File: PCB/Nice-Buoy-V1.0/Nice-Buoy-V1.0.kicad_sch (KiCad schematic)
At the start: 0 parts

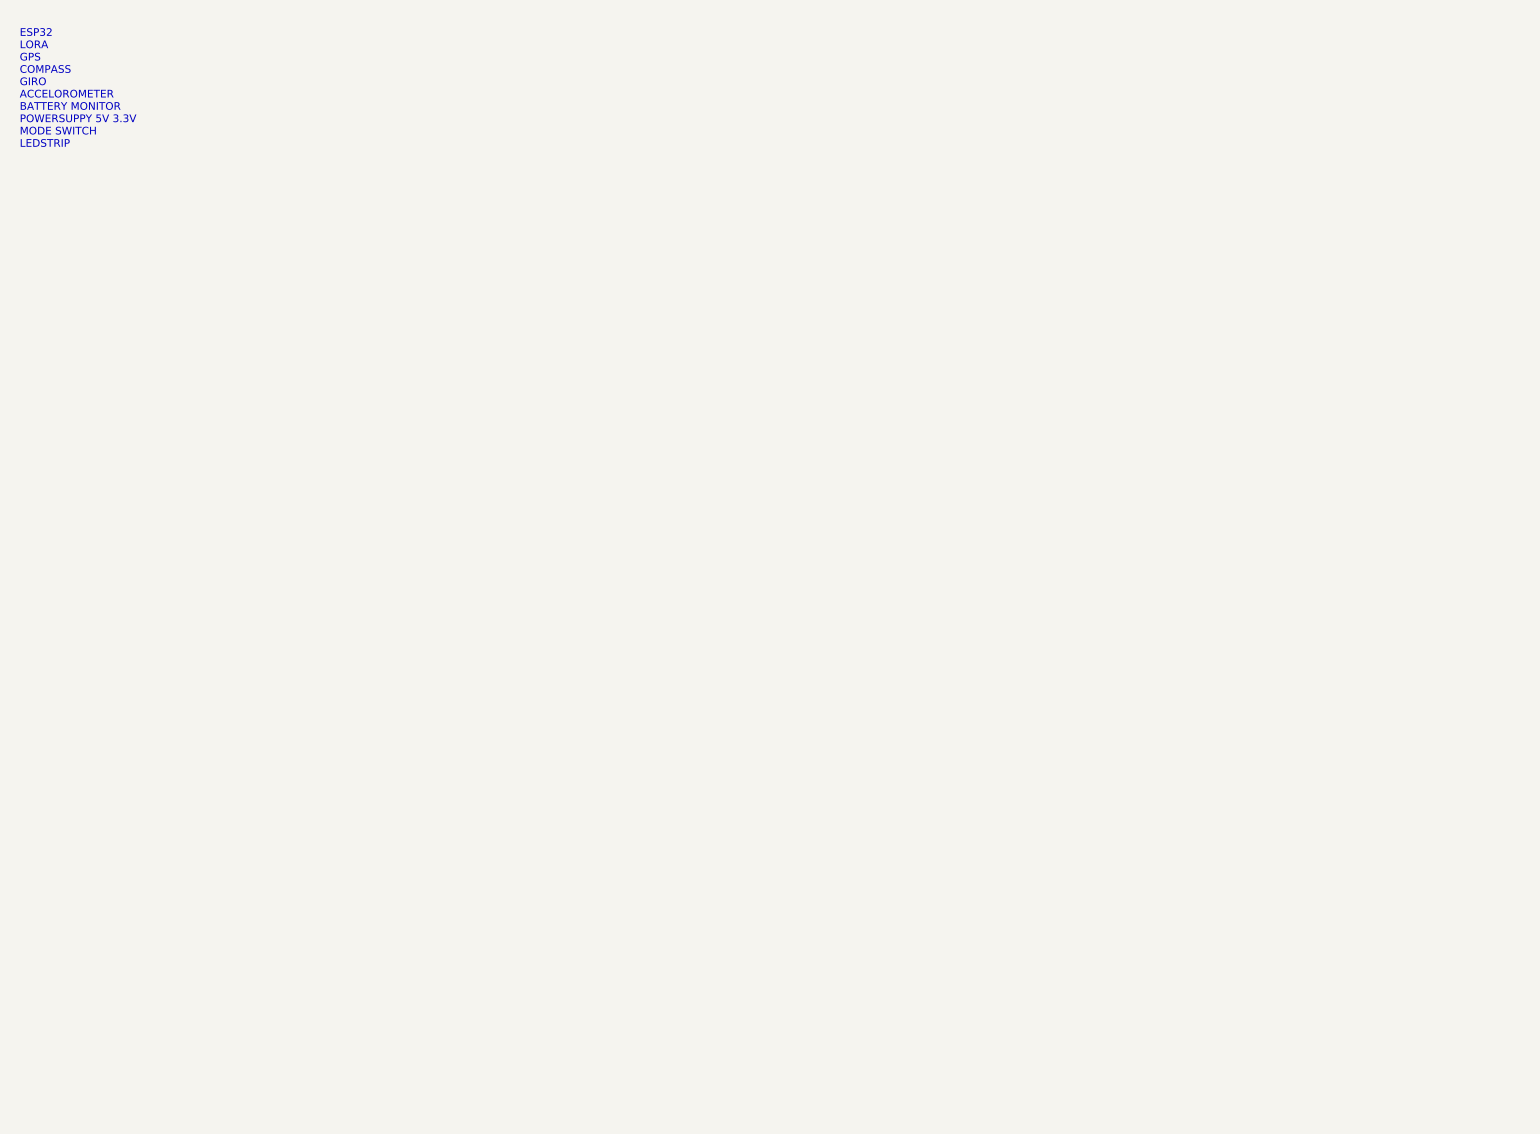
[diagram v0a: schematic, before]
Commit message: Compass BM150 is not okl. Next commit with LSM303
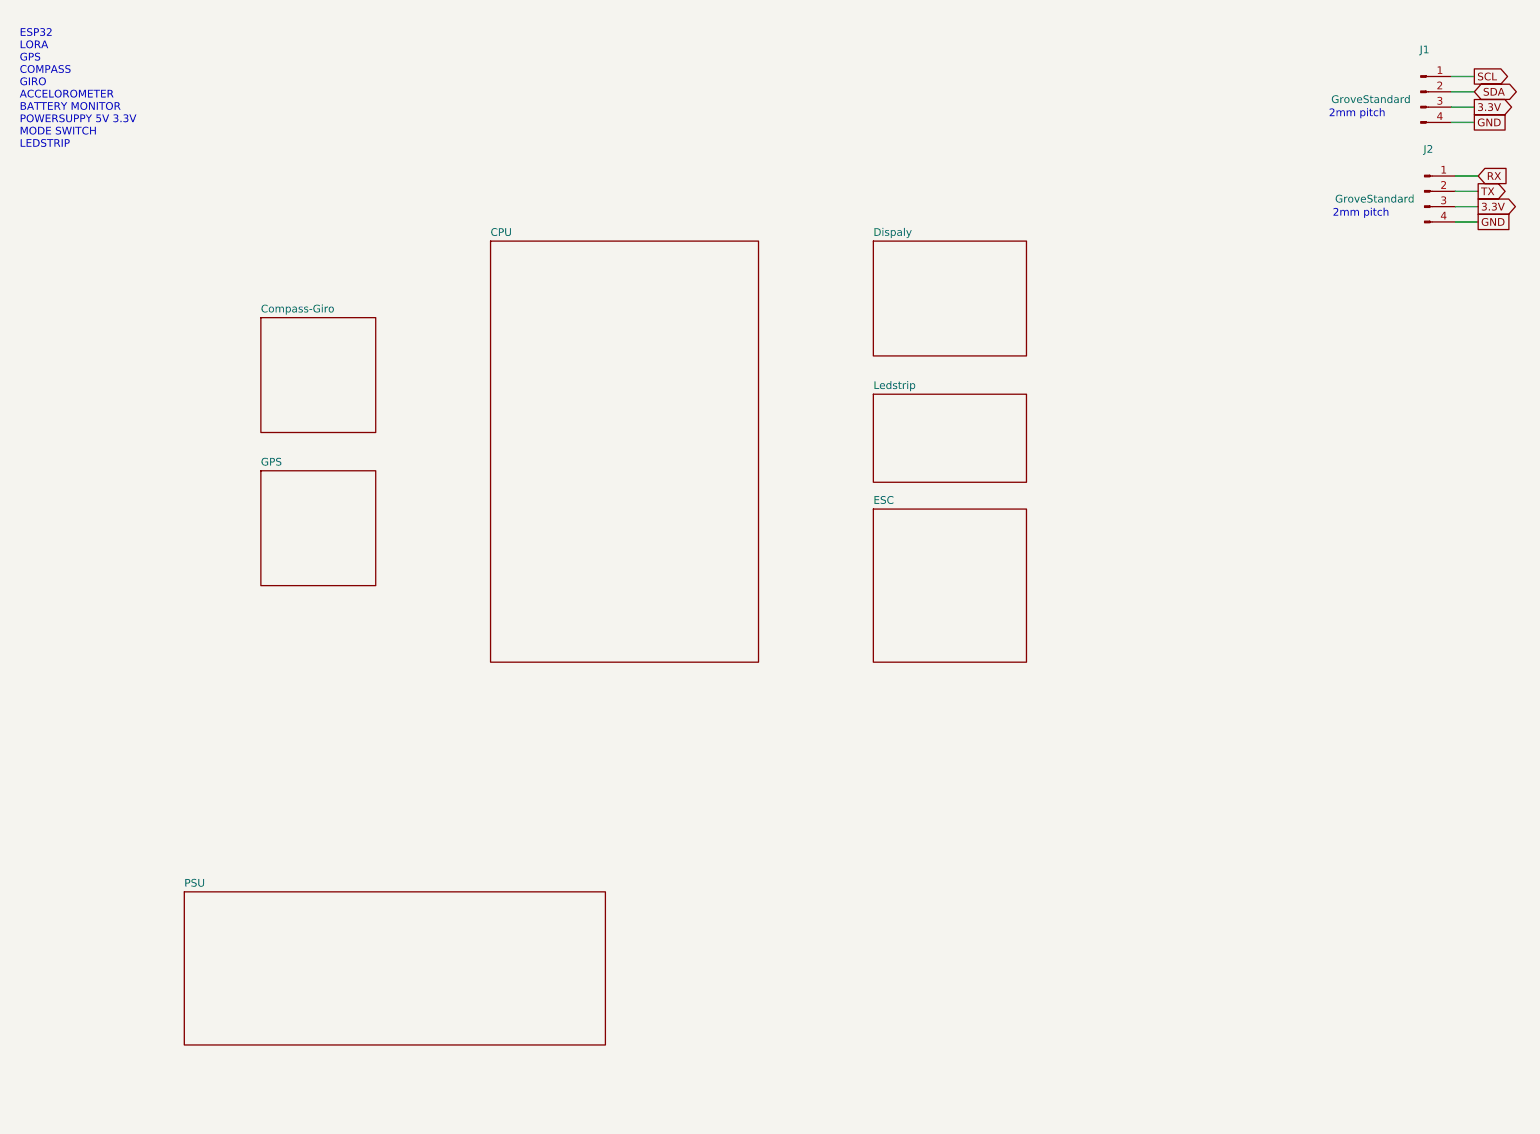
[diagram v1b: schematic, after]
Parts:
- added J1, J2: GroveStandard, symbol Connector:Conn_01x04_Pin
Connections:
- new net 3.3V: J1.3 (Pin_3), J2.3 (Pin_3)
- new net GND: J1.4 (Pin_4), J2.4 (Pin_4)
- new net RX: J2.1 (Pin_1)
- new net SCL: J1.1 (Pin_1)
- new net SDA: J1.2 (Pin_2)
- new net TX: J2.2 (Pin_2)
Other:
- added sheet CPU (CPU_sch.kicad_sch)
- added sheet Compass-Giro (Compass_sch.kicad_sch)
- added sheet Dispaly (Display_sch.kicad_sch)
- added sheet ESC (Esc_sch.kicad_sch)
- added sheet GPS (Gps_sch.kicad_sch)
- added sheet Ledstrip (Ledstrip_sch.kicad_sch)
- added sheet PSU (PSU_sch.kicad_sch)
- note added: "2mm pitch"
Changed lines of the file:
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@@
     (company "NicE Engineering")
+  )
+  (wire (pts (xy 255.27 40.005) (xy 259.08 40.005))
+    (stroke (width 0) (type default))
+  )
+  (wire (pts (xy 255.27 42.545) (xy 259.08 42.545))
+    (stroke (width 0) (type default))
+  )
+  (wire (pts (xy 254.635 26.035) (xy 258.445 26.035))
+    (stroke (width 0) (type default))
+  )
+  (wire (pts (xy 255.27 45.085) (xy 259.08 45.085))
+    (stroke (width 0) (type default))
+  )
+  (wire (pts (xy 254.635 28.575) (xy 258.445 28.575))
+    (stroke (width 0) (type default))
+  )
+  (wire (pts (xy 255.27 47.625) (xy 259.08 47.625))
+    (stroke (width 0) (type default))
+  )
+  (wire (pts (xy 254.635 31.115) (xy 258.445 31.115))
+    (stroke (width 0) (type default))
+  )
+  (wire (pts (xy 254.635 23.495) (xy 258.445 23.495))
+    (stroke (width 0) (type default))
+  )
+  (text "2mm pitch" (at 234.315 30.48 0)
+    (effects (font (size 1.27 1.27)) (justify left bottom))
+  )
+  (text "2mm pitch" (at 234.95 46.99 0)
+    (effects (font (size 1.27 1.27)) (justify left bottom))
   )
   (text "ESP32\nLORA\nGPS\nCOMPASS\nGIRO\nACCELOROMETER\nBATTERY MONITOR\nPOWERSUPPY 5V 3.3V\nMODE SWITCH\nLEDSTRIP\n"
@@
     (effects (font (size 1.27 1.27)) (justify left bottom))
   )
+  (global_label "3.3V" (shape output) (at 259.08 45.085 0) (fields_autoplaced)
+    (effects (font (size 1.27 1.27)) (justify left))
+    (property "Intersheetrefs" "${INTERSHEET_REFS}" (at 266.0982 45.085 0)
+      (effects (font (size 1.27 1.27)) (justify left) hide)
+    )
+  )
+  (global_label "GND" (shape passive) (at 258.445 31.115 0) (fields_autoplaced)
+    (effects (font (size 1.27 1.27)) (justify left))
+    (property "Intersheetrefs" "${INTERSHEET_REFS}" (at 264.11 31.115 0)
+      (effects (font (size 1.27 1.27)) (justify left) hide)
+    )
+  )
+  (global_label "RX" (shape input) (at 259.08 40.005 0) (fields_autoplaced)
+    (effects (font (size 1.27 1.27)) (justify left))
+    (property "Intersheetrefs" "${INTERSHEET_REFS}" (at 264.4653 40.005 0)
+      (effects (font (size 1.27 1.27)) (justify left) hide)
+    )
+  )
+  (global_label "3.3V" (shape output) (at 258.445 28.575 0) (fields_autoplaced)
+    (effects (font (size 1.27 1.27)) (justify left))
+    (property "Intersheetrefs" "${INTERSHEET_REFS}" (at 265.4632 28.575 0)
+      (effects (font (size 1.27 1.27)) (justify left) hide)
+    )
+  )
+  (global_label "TX" (shape output) (at 259.08 42.545 0) (fields_autoplaced)
+    (effects (font (size 1.27 1.27)) (justify left))
+    (property "Intersheetrefs" "${INTERSHEET_REFS}" (at 264.1629 42.545 0)
+      (effects (font (size 1.27 1.27)) (justify left) hide)
+    )
+  )
+  (global_label "GND" (shape passive) (at 259.08 47.625 0) (fields_autoplaced)
+    (effects (font (size 1.27 1.27)) (justify left))
+    (property "Intersheetrefs" "${INTERSHEET_REFS}" (at 264.745 47.625 0)
+      (effects (font (size 1.27 1.27)) (justify left) hide)
+    )
+  )
+  (global_label "SCL" (shape output) (at 258.445 23.495 0) (fields_autoplaced)
+    (effects (font (size 1.27 1.27)) (justify left))
+    (property "Intersheetrefs" "${INTERSHEET_REFS}" (at 264.8584 23.495 0)
+      (effects (font (size 1.27 1.27)) (justify left) hide)
+    )
+  )
+  (global_label "SDA" (shape bidirectional) (at 258.445 26.035 0) (fields_autoplaced)
+    (effects (font (size 1.27 1.27)) (justify left))
+    (property "Intersheetrefs" "${INTERSHEET_REFS}" (at 266.0302 26.035 0)
+      (effects (font (size 1.27 1.27)) (justify left) hide)
+    )
+  )
+  (symbol (lib_id "Connector:Conn_01x04_Pin") (at 249.555 26.035 0) (unit 1)
+    (in_bom yes) (on_board yes) (dnp no)
+    (property "Reference" "J1" (at 250.19 19.05 0)
+      (effects (font (size 1.27 1.27)))
+    )
+    (property "Value" "GroveStandard" (at 241.3 27.305 0)
+      (effects (font (size 1.27 1.27)))
+    )
+    (property "Footprint" "" (at 249.555 26.035 0)
+      (effects (font (size 1.27 1.27)) hide)
+    )
+    (property "Datasheet" "~" (at 249.555 26.035 0)
+      (effects (font (size 1.27 1.27)) hide)
+    )
+    (pin "1")
+    (pin "2")
+    (pin "3")
+    (pin "4")
+    (instances
+      (project "Nice-Buoy-V1.0"
+        (path "/77bea089-a6ae-4a6f-b95b-7a9010ad7c5d"
+          (reference "J1") (unit 1)
+        )
+      )
+    )
+  )
+  (symbol (lib_id "Connector:Conn_01x04_Pin") (at 250.19 42.545 0) (unit 1)
+    (in_bom yes) (on_board yes) (dnp no)
+    (property "Reference" "J2" (at 250.825 35.56 0)
+      (effects (font (size 1.27 1.27)))
+    )
+    (property "Value" "GroveStandard" (at 241.935 43.815 0)
+      (effects (font (size 1.27 1.27)))
+    )
+    (property "Footprint" "" (at 250.19 42.545 0)
+      (effects (font (size 1.27 1.27)) hide)
+    )
+    (property "Datasheet" "~" (at 250.19 42.545 0)
+      (effects (font (size 1.27 1.27)) hide)
+    )
+    (pin "1")
+    (pin "2")
+    (pin "3")
+    (pin "4")
+    (instances
+      (project "Nice-Buoy-V1.0"
+        (path "/77bea089-a6ae-4a6f-b95b-7a9010ad7c5d"
+          (reference "J2") (unit 1)
+        )
+      )
+    )
+  )
+  (sheet (at 158.75 50.8) (size 25.4 19.05) (fields_autoplaced)
+    (stroke (width 0.1524) (type solid))
+    (fill (color 0 0 0 0.0000))
+    (property "Sheetname" "Dispaly" (at 158.75 50.0884 0)
+      (effects (font (size 1.27 1.27)) (justify left bottom))
+    )
+    (property "Sheetfile" "Display_sch.kicad_sch" (at 158.75 70.4346 0)
+      (effects (font (size 1.27 1.27)) (justify left top) hide)
+    )
+    (instances
+      (project "Nice-Buoy-V1.0"
+        (path "/77bea089-a6ae-4a6f-b95b-7a9010ad7c5d" (page "8"))
+      )
+    )
+  )
+  (sheet (at 95.25 50.8) (size 44.45 69.85) (fields_autoplaced)
+    (stroke (width 0.1524) (type solid))
+    (fill (color 0 0 0 0.0000))
+    (property "Sheetname" "CPU" (at 95.25 50.0884 0)
+      (effects (font (size 1.27 1.27)) (justify left bottom))
+    )
+    (property "Sheetfile" "CPU_sch.kicad_sch" (at 95.25 121.2346 0)
+      (effects (font (size 1.27 1.27)) (justify left top) hide)
+    )
+    (instances
+      (project "Nice-Buoy-V1.0"
+        (path "/77bea089-a6ae-4a6f-b95b-7a9010ad7c5d" (page "2"))
+      )
+    )
+  )
+  (sheet (at 158.75 76.2) (size 25.4 14.605) (fields_autoplaced)
+    (stroke (width 0.1524) (type solid))
+    (fill (color 0 0 0 0.0000))
+    (property "Sheetname" "Ledstrip" (at 158.75 75.4884 0)
+      (effects (font (size 1.27 1.27)) (justify left bottom))
+    )
+    (property "Sheetfile" "Ledstrip_sch.kicad_sch" (at 158.75 91.3896 0)
+      (effects (font (size 1.27 1.27)) (justify left top) hide)
+    )
+    (instances
+      (project "Nice-Buoy-V1.0"
+        (path "/77bea089-a6ae-4a6f-b95b-7a9010ad7c5d" (page "9"))
+      )
+    )
+  )
+  (sheet (at 57.15 88.9) (size 19.05 19.05) (fields_autoplaced)
+    (stroke (width 0.1524) (type solid))
+    (fill (color 0 0 0 0.0000))
+    (property "Sheetname" "GPS" (at 57.15 88.1884 0)
+      (effects (font (size 1.27 1.27)) (justify left bottom))
+    )
+    (property "Sheetfile" "Gps_sch.kicad_sch" (at 57.15 108.5346 0)
+      (effects (font (size 1.27 1.27)) (justify left top) hide)
+    )
+    (instances
+      (project "Nice-Buoy-V1.0"
+        (path "/77bea089-a6ae-4a6f-b95b-7a9010ad7c5d" (page "7"))
+      )
+    )
+  )
+  (sheet (at 57.15 63.5) (size 19.05 19.05) (fields_autoplaced)
+    (stroke (width 0.1524) (type solid))
+    (fill (color 0 0 0 0.0000))
+    (property "Sheetname" "Compass-Giro" (at 57.15 62.7884 0)
+      (effects (font (size 1.27 1.27)) (justify left bottom))
+    )
+    (property "Sheetfile" "Compass_sch.kicad_sch" (at 57.15 83.1346 0)
+      (effects (font (size 1.27 1.27)) (justify left top) hide)
+    )
+    (instances
+      (project "Nice-Buoy-V1.0"
+        (path "/77bea089-a6ae-4a6f-b95b-7a9010ad7c5d" (page "5"))
+      )
+    )
+  )
+  (sheet (at 44.45 158.75) (size 69.85 25.4) (fields_autoplaced)
+    (stroke (width 0.1524) (type solid))
+    (fill (color 0 0 0 0.0000))
+    (property "Sheetname" "PSU" (at 44.45 158.0384 0)
+      (effects (font (size 1.27 1.27)) (justify left bottom))
+    )
+    (property "Sheetfile" "PSU_sch.kicad_sch" (at 44.45 184.7346 0)
+      (effects (font (size 1.27 1.27)) (justify left top) hide)
+    )
+    (instances
+      (project "Nice-Buoy-V1.0"
+        (path "/77bea089-a6ae-4a6f-b95b-7a9010ad7c5d" (page "4"))
+      )
+    )
+  )
+  (sheet (at 158.75 95.25) (size 25.4 25.4) (fields_autoplaced)
+    (stroke (width 0.1524) (type solid))
+    (fill (color 0 0 0 0.0000))
+    (property "Sheetname" "ESC" (at 158.75 94.5384 0)
+      (effects (font (size 1.27 1.27)) (justify left bottom))
+    )
+    (property "Sheetfile" "Esc_sch.kicad_sch" (at 158.75 121.2346 0)
+      (effects (font (size 1.27 1.27)) (justify left top) hide)
+    )
+    (instances
+      (project "Nice-Buoy-V1.0"
+        (path "/77bea089-a6ae-4a6f-b95b-7a9010ad7c5d" (page "6"))
+      )
+    )
+  )
   (sheet_instances

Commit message: Lots of 3d parts added
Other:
- note added: "ESP32 LORA GPS COMPASS GIRO ACCELOROMETER BATTERY MONITOR POWERSUPPY 5V 3.3V MODE SWITCH LEDSTRIP Lipo monitoring"
- note removed: "ESP32 LORA GPS COMPASS GIRO ACCELOROMETER BATTERY MONITOR POWERSUPPY 5V 3.3V MODE SWITCH LEDSTRIP"
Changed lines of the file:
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@@
     (effects (font (size 1.27 1.27)) (justify left bottom))
   )
-  (text "ESP32\nLORA\nGPS\nCOMPASS\nGIRO\nACCELOROMETER\nBATTERY MONITOR\nPOWERSUPPY 5V 3.3V\nMODE SWITCH\nLEDSTRIP\n"
+  (text "ESP32\nLORA\nGPS\nCOMPASS\nGIRO\nACCELOROMETER\nBATTERY MONITOR\nPOWERSUPPY 5V 3.3V\nMODE SWITCH\nLEDSTRIP\nLipo monitoring\n"
     (at 17.145 35.56 0)
     (effects (font (size 1.27 1.27)) (justify left bottom))

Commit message: Schematic and docs updated
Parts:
- renumbered J1 to J201, J2 to J202
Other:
- added sheet Accumonitor (untitled.kicad_sch)
- note added: "ESP32 LORA GPS COMPASS GIRO ACCELOROMETER BATTERY MONITOR POWERSUPPY 12V 5V 3.3V MODE SWITCH LEDSTRIP Lipo monitoring"
- note removed: "ESP32 LORA GPS COMPASS GIRO ACCELOROMETER BATTERY MONITOR POWERSUPPY 5V 3.3V MODE SWITCH LEDSTRIP Lipo monitoring"
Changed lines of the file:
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@@
     (effects (font (size 1.27 1.27)) (justify left bottom))
   )
-  (text "ESP32\nLORA\nGPS\nCOMPASS\nGIRO\nACCELOROMETER\nBATTERY MONITOR\nPOWERSUPPY 5V 3.3V\nMODE SWITCH\nLEDSTRIP\nLipo monitoring\n"
+  (text "ESP32\nLORA\nGPS\nCOMPASS\nGIRO\nACCELOROMETER\nBATTERY MONITOR\nPOWERSUPPY 12V 5V 3.3V\nMODE SWITCH\nLEDSTRIP\nLipo monitoring\n"
     (at 17.145 35.56 0)
     (effects (font (size 1.27 1.27)) (justify left bottom))
@@
   (symbol (lib_id "Connector:Conn_01x04_Pin") (at 249.555 26.035 0) (unit 1)
     (in_bom yes) (on_board yes) (dnp no)
-    (property "Reference" "J1" (at 250.19 19.05 0)
+    (property "Reference" "J201" (at 250.19 19.05 0)
       (effects (font (size 1.27 1.27)))
     )
@@
       (project "Nice-Buoy-V1.0"
         (path "/77bea089-a6ae-4a6f-b95b-7a9010ad7c5d"
-          (reference "J1") (unit 1)
+          (reference "J201") (unit 1)
         )
       )
@@
   (symbol (lib_id "Connector:Conn_01x04_Pin") (at 250.19 42.545 0) (unit 1)
     (in_bom yes) (on_board yes) (dnp no)
-    (property "Reference" "J2" (at 250.825 35.56 0)
+    (property "Reference" "J202" (at 250.825 35.56 0)
       (effects (font (size 1.27 1.27)))
     )
@@
       (project "Nice-Buoy-V1.0"
         (path "/77bea089-a6ae-4a6f-b95b-7a9010ad7c5d"
-          (reference "J2") (unit 1)
+          (reference "J202") (unit 1)
         )
       )
     )
+  )
+  (sheet (at 120.65 158.75) (size 44.45 25.4) (fields_autoplaced)
+    (stroke (width 0.1524) (type solid))
+    (fill (color 0 0 0 0.0000))
+    (property "Sheetname" "Accumonitor" (at 120.65 158.0384 0)
+      (effects (font (size 1.27 1.27)) (justify left bottom))
+    )
+    (property "Sheetfile" "untitled.kicad_sch" (at 120.65 184.7346 0)
+      (effects (font (size 1.27 1.27)) (justify left top) hide)
+    )
+    (instances
+      (project "Nice-Buoy-V1.0"
+        (path "/77bea089-a6ae-4a6f-b95b-7a9010ad7c5d" (page "9"))
+      )
+    )

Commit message: Many changes in schematics
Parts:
- removed J201, J202: GroveStandard, symbol Connector:Conn_01x04_Pin
- added H1, H2, H3, H4: MountingHole, A_Mechanical:NPTH_M3, symbol Mechanical:MountingHole
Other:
- removed sheet Dispaly
- added sheet Gyroscop (Gyroscoop.kicad_sch)
- added sheet Lora (Lora.kicad_sch)
- sheet Accumonitor ports: added SCL, SDA; removed none
- sheet CPU ports: added ESC_BB, ESC_SB, GPSRX, GPSTX, LEDSTRIP_BB, LEDSTRIP_SB, RADIO_[1..6], SCL, SDA; removed none
- sheet Compass-Giro ports: added SCL, SDA; removed none
- sheet ESC ports: added ESC_BB, ESC_SB; removed none
- sheet GPS ports: added RX, TX; removed none
- sheet Ledstrip ports: added LEDSTRIP_BB, LEDSTRIP_SB; removed none
- note added: "100"
- note added: "200"
- note added: "300"
- note added: "400"
- note added: "500"
- note added: "600"
- note added: "700"
- note added: "800"
- note removed: "2mm pitch"
